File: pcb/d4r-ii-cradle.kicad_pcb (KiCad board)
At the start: 2 copper layers, 36 x 36 mm, 31 parts, among them P1 CONN_02X06, P2 CONN_01X04, P3 CONN_01X02, Q1 Q_NMOS_GSD, Q2 Q_NMOS_GSD

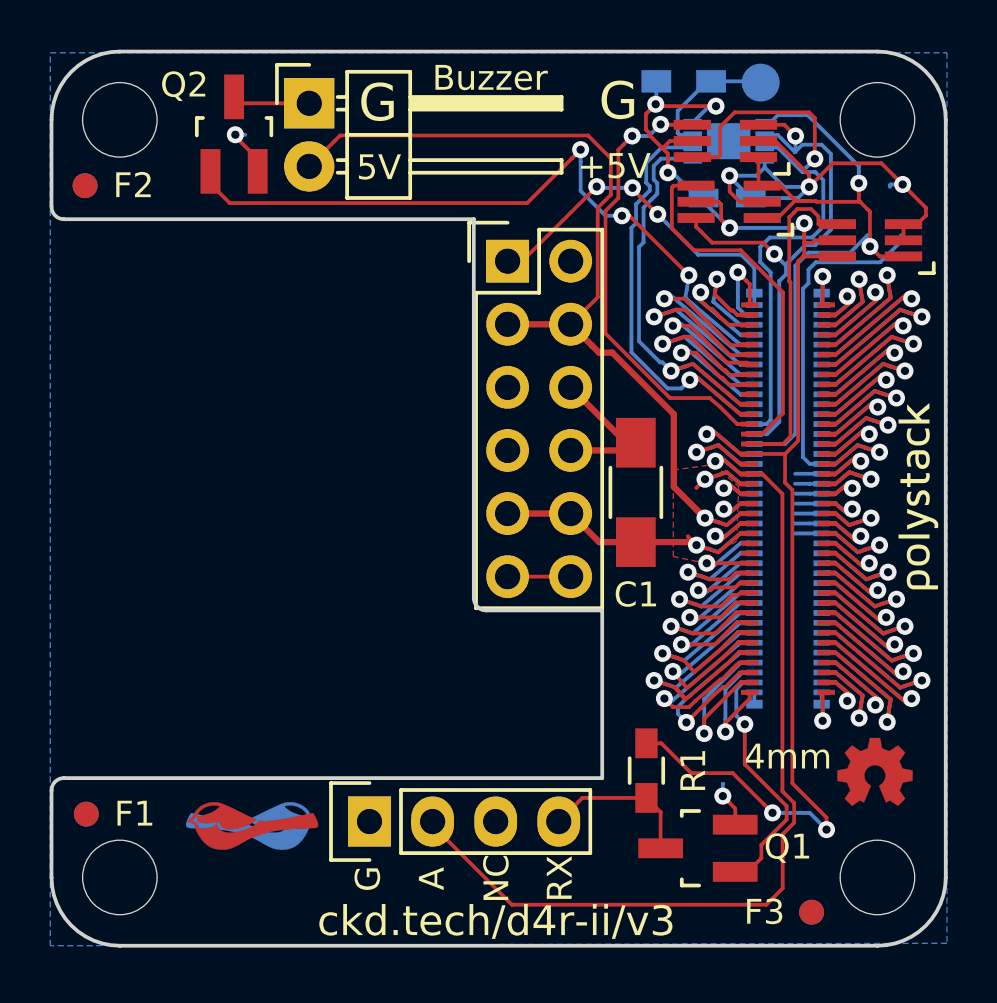
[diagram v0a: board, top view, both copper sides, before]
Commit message: Update polystack logo to bold variant and bump version number.
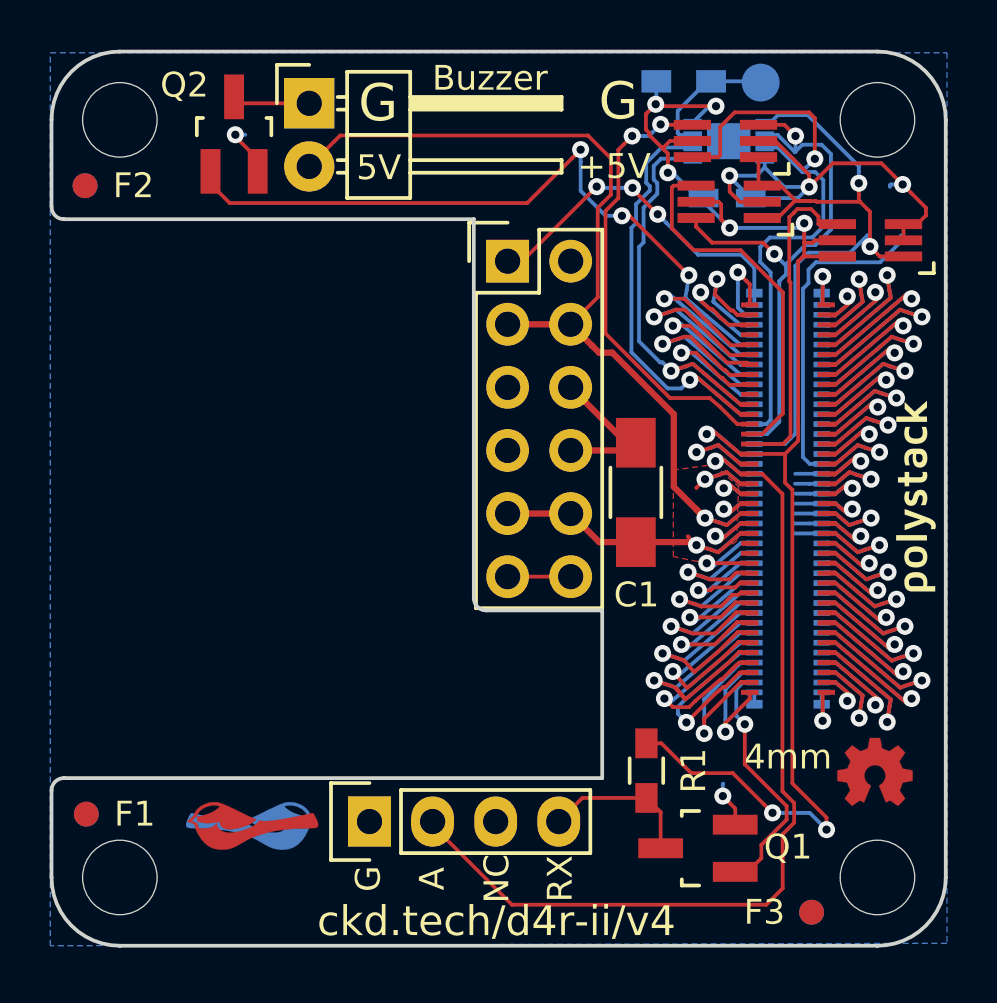
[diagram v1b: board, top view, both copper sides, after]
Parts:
- svg2mod (x2): footprint polystack:polystack-medium-0.4 -> polystack:polystack-bold-0.4
- moved svg2mod 0.10 mm to (164.8, 107.9) (x2)
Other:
- board text added: "ckd.tech/d4r-ii/v4"
- board text removed: "ckd.tech/d4r-ii/v3"

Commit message: Add license information to many files. PCB design files are CC-BY and code is MIT license.
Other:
- board text added: "Copyright 2016 Chickadee Tech LLC, <add attributions here> This work is licensed under the Creative Commons Attribution 4.0 International License. To view a copy of this license, visit http://creativecommons.org/licenses/by/4.0/ or send a letter to Creative Commons, PO Box 1866, Mountain View, CA 94042, USA."
- board text added: "Remove all Chickadee Tech LLC trademarks before making your own board. The Chickadee logo and Polystack logo are owned by Chickadee Tech LLC. You may license the Polystack logo for free by emailing support@chickadee.tech and receiving express written permission from Chickadee Tech LLC."
- board text added: "The gear logo is a mark designating open source hardware. Remove it if your design does not comply with the open source hardware definition."
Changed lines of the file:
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@@
     (area 118.127143 74.1 240.357143 178)
     (thickness 1.6)
-    (drawings 54)
+    (drawings 62)
     (tracks 1006)
     (zones 0)
@@
     (40 Dwgs.User user)
     (41 Cmts.User user)
-    (42 Eco1.User user hide)
+    (42 Eco1.User user)
     (43 Eco2.User user hide)
     (44 Edge.Cuts user)
@@
       (xy 2.990233 -0.444493)) (layer B.SilkS) (width 0))
   )
+  (gr_line (start 165.28 119.06) (end 170.55 121.69) (layer Cmts.User) (width 0.2))
+  (gr_text "The gear logo is a mark designating open\nsource hardware. Remove it if your design\ndoes not comply with the open source\nhardware definition." (at 170.92 121.69) (layer Cmts.User)
+    (effects (font (size 1.5 1.5) (thickness 0.3)) (justify left))
+  )
+  (gr_line (start 111.94 128.22) (end 163.27 107.89) (layer Cmts.User) (width 0.2))
+  (gr_line (start 136.66 122.82) (end 111.94 128.22) (layer Cmts.User) (width 0.2))
+  (gr_text "Remove all Chickadee Tech LLC trademarks\nbefore making your own board. The\nChickadee logo and Polystack logo\nare owned by Chickadee Tech LLC.\n\nYou may license the Polystack logo for\nfree by emailing support@chickadee.tech\nand receiving express written permission\nfrom Chickadee Tech LLC." (at 88.22 139.77) (layer Cmts.User)
+    (effects (font (size 1.5 1.5) (thickness 0.3)) (justify left))
+  )
+  (gr_text "Copyright 2016 Chickadee Tech LLC, <add attributions here>\n\nThis work is licensed under the Creative Commons Attribution 4.0 International License.\nTo view a copy of this license, visit http://creativecommons.org/licenses/by/4.0/\nor send a letter to Creative Commons, PO Box 1866, Mountain View, CA 94042, USA." (at 178.74 174.07) (layer Cmts.User)
+    (effects (font (size 1.5 1.5) (thickness 0.3)) (justify left))
+  )
+  (gr_line (start 153.5 89.72) (end 153.5 92.55) (layer Dwgs.User) (width 0.2))
+  (dimension 12.440326 (width 0.3) (layer Dwgs.User)
+    (gr_text "12.440 mm" (at 159.638023 86.307294 0.4145120732) (layer Dwgs.User)
+      (effects (font (size 1.5 1.5) (thickness 0.3)))
+    )
+    (feature1 (pts (xy 165.88 89.3) (xy 165.848257 84.91233)))
+    (feature2 (pts (xy 153.44 89.39) (xy 153.408257 85.00233)))
+    (crossbar (pts (xy 153.42779 87.702259) (xy 165.86779 87.612259)))
+    (arrow1a (pts (xy 165.86779 87.612259) (xy 164.745558 88.206814)))
+    (arrow1b (pts (xy 165.86779 87.612259) (xy 164.737073 87.034003)))
+    (arrow2a (pts (xy 153.42779 87.702259) (xy 154.558507 88.280515)))
+    (arrow2b (pts (xy 153.42779 87.702259) (xy 154.550022 87.107704)))
+  )
   (gr_text RX (at 150.475 123.3 90) (layer B.SilkS)
     (effects (font (size 1 1) (thickness 0.15)) (justify mirror))
@@
   (gr_line (start 166 92.75) (end 166 123.25) (angle 90) (layer Edge.Cuts) (width 0.15))
   (gr_line (start 132.75 90) (end 163.25 90) (angle 90) (layer Edge.Cuts) (width 0.15))
-  (gr_text d4r-ii-cradle (at 187.25 174.25) (layer Cmts.User)
-    (effects (font (size 5 5) (thickness 0.5)) (justify left))
+  (gr_text d4r-ii-cradle (at 187.07 189.95) (layer Cmts.User)
+    (effects (font (size 3 3) (thickness 0.5)) (justify left))
   )
   (segment (start 162.95 97.849974) (end 162.95 96.45) (width 0.1524) (layer F.Cu) (net 1))
